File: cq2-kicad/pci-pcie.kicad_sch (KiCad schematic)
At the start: 52 parts, among them U6 PI7C9X111, U7 24LC02B

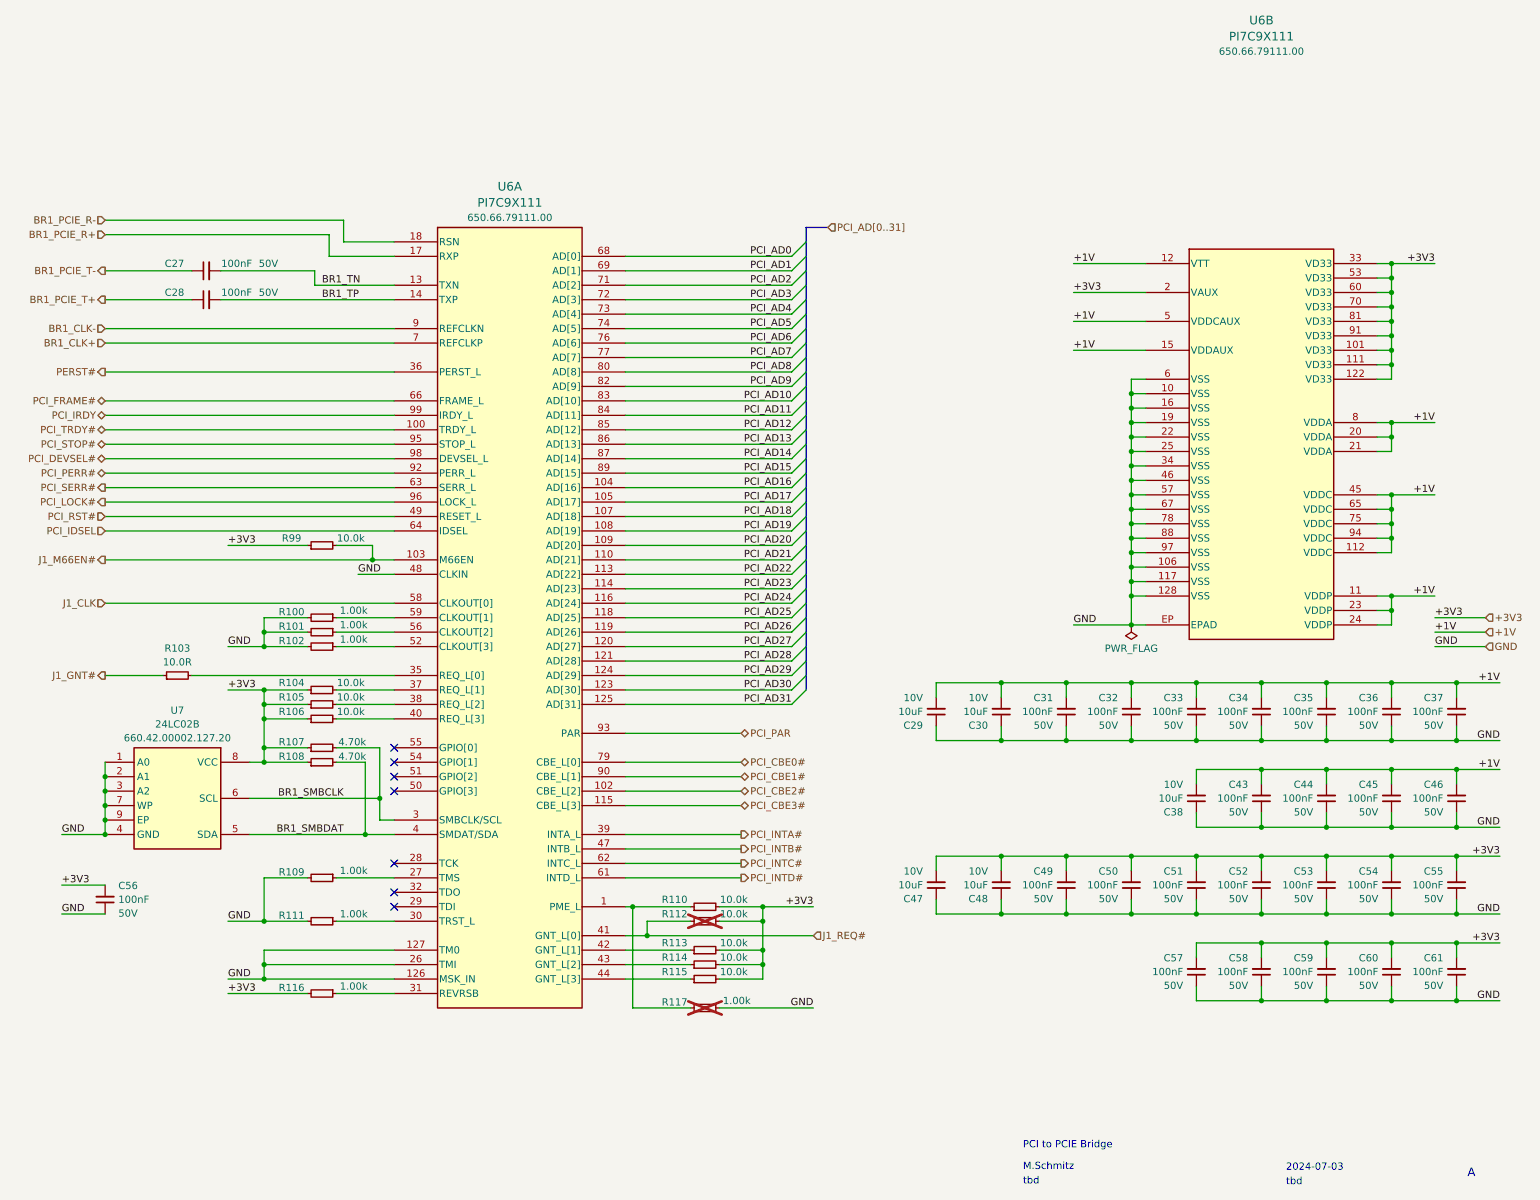
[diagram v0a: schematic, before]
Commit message: drc checked before panalization
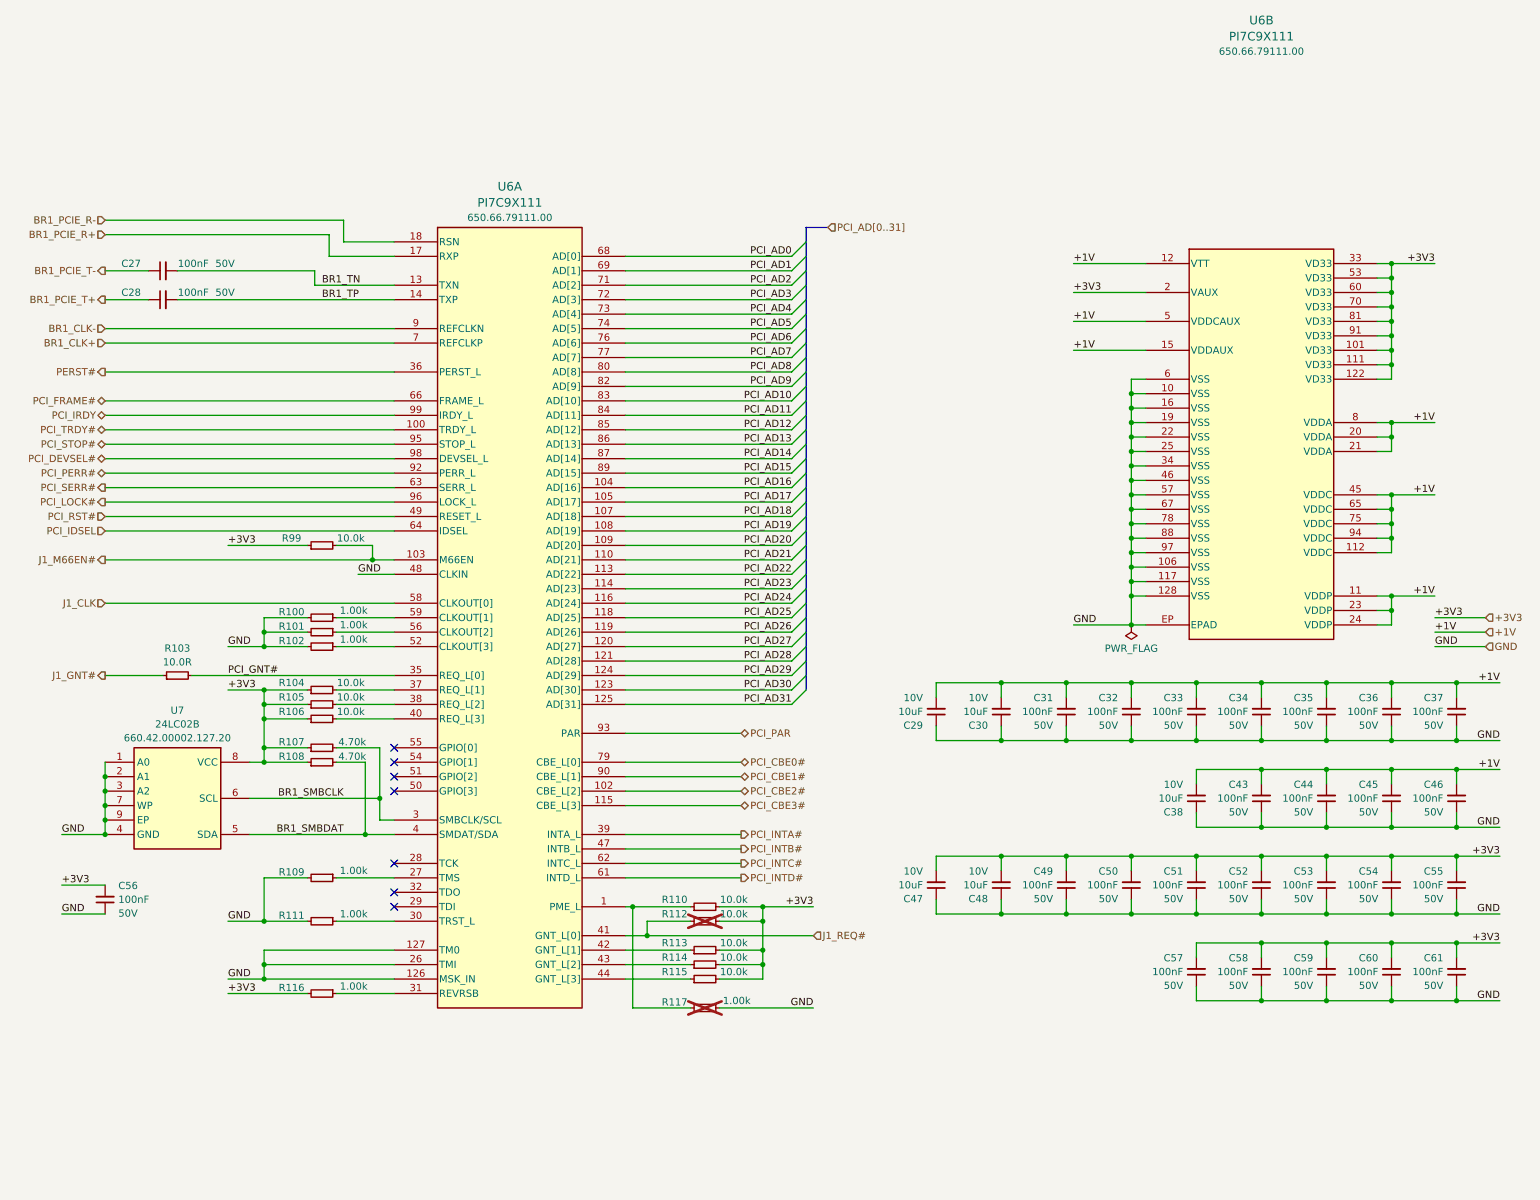
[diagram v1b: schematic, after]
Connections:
- net PCI_GNT#: now reaches R103.2, U6.35 (REQ_L[0])
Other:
- note removed: "2024-07-03"
- note removed: "A"
- note removed: "M.Schmitz"
- note removed: "PCI to PCIE Bridge"
- note removed: "tbd"
- title: (none) -> CQ2
- moved on the sheet: C27, C28
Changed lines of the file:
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@@
 	(paper "A4")
 	(title_block
-		(date "2024-07-17")
+		(title "CQ2")
+		(date "2024-07-31")
 		(rev "0")
+		(comment 1 "PCI to PCIE Bridge")
+		(comment 2 "Manfred Schmitz")
+		(comment 3 "tbd")
+		(comment 4 "202-07-03")
+		(comment 5 "tbd")
+		(comment 6 "A")
 	)
 	(junction
@@
 	(wire
 		(pts
-			(xy 49.53 38.1) (xy 80.01 38.1)
+			(xy 41.91 38.1) (xy 80.01 38.1)
 		)
 		(stroke
@@
 	(wire
 		(pts
-			(xy 29.21 33.02) (xy 44.45 33.02)
+			(xy 29.21 33.02) (xy 36.83 33.02)
 		)
 		(stroke
@@
 	(wire
 		(pts
-			(xy 29.21 38.1) (xy 44.45 38.1)
+			(xy 29.21 38.1) (xy 36.83 38.1)
 		)
 		(stroke
@@
 	(wire
 		(pts
-			(xy 66.04 33.02) (xy 49.53 33.02)
+			(xy 66.04 33.02) (xy 41.91 33.02)
 		)
 		(stroke
@@
 		)
 	)
-	(text "M.Schmitz"
-		(exclude_from_sim no)
-		(at 190.5 191.262 0)
-		(effects
-			(font
-				(size 1.27 1.27)
-			)
-			(justify left bottom)
-		)
-	)
-	(text "A"
-		(exclude_from_sim no)
-		(at 268.605 192.532 0)
-		(effects
-			(font
-				(size 1.4986 1.4986)
-			)
-			(justify left bottom)
-		)
-	)
-	(text "tbd"
-		(exclude_from_sim no)
-		(at 190.5 193.802 0)
-		(effects
-			(font
-				(size 1.27 1.27)
-			)
-			(justify left bottom)
-		)
-	)
-	(text "PCI to PCIE Bridge"
-		(exclude_from_sim no)
-		(at 190.5 187.452 0)
-		(effects
-			(font
-				(size 1.27 1.27)
-			)
-			(justify left bottom)
-		)
-	)
-	(text "tbd"
-		(exclude_from_sim no)
-		(at 236.728 193.929 0)
-		(effects
-			(font
-				(size 1.27 1.27)
-			)
-			(justify left bottom)
-		)
-	)
-	(text "2024-07-03"
-		(exclude_from_sim no)
-		(at 236.728 191.389 0)
-		(effects
-			(font
-				(size 1.27 1.27)
-			)
-			(justify left bottom)
-		)
-	)
 	(label "PCI_AD3"
 		(at 149.86 38.1 180)
@@
 		)
 	)
+	(label "PCI_GNT#"
+		(at 50.8 104.14 0)
+		(fields_autoplaced yes)
+		(effects
+			(font
+				(size 1.27 1.27)
+			)
+			(justify left bottom)
+		)
+	)
 	(label "PCI_AD30"
 		(at 149.86 106.68 180)
@@
 		)
 	)
+	(netclass_flag ""
+		(length 1.28)
+		(shape round)
+		(at 57.15 38.1 0)
+		(effects
+			(font
+				(size 1.27 1.27)
+			)
+			(justify left bottom)
+		)
+		(property "Netclass" "PCIE"
+			(at 57.658 36.83 0)
+			(effects
+				(font
+					(size 1.27 1.27)
+					(italic yes)
+				)
+				(justify left)
+			)
+		)
+	)
+	(netclass_flag ""
+		(length 1.28)
+		(shape round)
+		(at 57.15 33.02 0)
+		(effects
+			(font
+				(size 1.27 1.27)
+			)
+			(justify left bottom)
+		)
+		(property "Netclass" "PCIE"
+			(at 57.658 31.75 0)
+			(effects
+				(font
+					(size 1.27 1.27)
+					(italic yes)
+				)
+				(justify left)
+			)
+		)
+	)
 	(symbol
 		(lib_id "ci4rail-database:capacitors/86")
@@
 	(symbol
 		(lib_id "ci4rail-database:capacitors/86")
-		(at 46.99 33.02 90)
+		(at 39.37 33.02 90)
 		(unit 1)
 		(exclude_from_sim no)
@@
 		(dnp no)
 		(property "Reference" "C27"
-			(at 41.402 31.75 90)
+			(at 33.782 31.75 90)
 			(effects
 				(font
@@
 		)
 		(property "Value" "100nF"
-			(at 52.324 31.75 90)
+			(at 44.704 31.75 90)
 			(effects
 				(font
@@
 		)
 		(property "Footprint" "0-standard:0402-capacitor"
-			(at 46.99 33.02 0)
+			(at 39.37 33.02 0)
 			(effects
 				(font
@@
 		)
 		(property "Datasheet" ""
-			(at 46.99 33.02 0)
+			(at 39.37 33.02 0)
 			(effects
 				(font
@@
 		)
 		(property "Description" "Multilayer Ceramic Capacitors"
-			(at 46.99 33.02 0)
+			(at 39.37 33.02 0)
 			(effects
 				(font
@@
 		)
 		(property "Value1" "+/-10 %"
-			(at 46.99 33.02 0)
+			(at 39.37 33.02 0)
 			(effects
 				(font
@@
 		)
 		(property "Value2" "50V"
-			(at 57.912 31.75 90)
+			(at 50.292 31.75 90)
 			(effects
 				(font
@@
 		)
 		(property "Value3" "X5R/X7R"
-			(at 46.99 33.02 0)
+			(at 39.37 33.02 0)
 			(effects
 				(font
@@
 		)
 		(property "Value4" ""
-			(at 46.99 33.02 0)
+			(at 39.37 33.02 0)
 			(effects
 				(font
@@
 		)
 		(property "MPN" "n/a"
-			(at 46.99 33.02 0)
+			(at 39.37 33.02 0)
 			(effects
 				(font
@@
 		)
 		(property "MPN1" ""
-			(at 46.99 33.02 0)
+			(at 39.37 33.02 0)
 			(effects
 				(font
@@
 		)
 		(property "MPN2" ""
-			(at 46.99 33.02 0)
+			(at 39.37 33.02 0)
 			(effects
 				(font
@@
 		)
 		(property "LTB" "9999"
-			(at 46.99 33.02 0)
+			(at 39.37 33.02 0)
 			(effects
 				(font
@@
 		)
 		(property "ERP1" "M120-00060-00"
-			(at 46.99 33.02 0)
+			(at 39.37 33.02 0)
 			(effects
 				(font
@@
 		)
 		(property "ERP2" "110.42.410.050.0"
-			(at 46.99 33.02 0)
+			(at 39.37 33.02 0)
 			(effects
 				(font
@@
 		)
 		(property "Cost" "0.02"
-			(at 46.99 33.02 0)
+			(at 39.37 33.02 0)
 			(effects
 				(font
@@
 		)
 		(property "Lifecycle" "released"
-			(at 46.99 33.02 0)
+			(at 39.37 33.02 0)
 			(effects
 				(font
@@
 		)
 		(property "Outline" "SMT 0402"
-			(at 46.99 33.02 0)
+			(at 39.37 33.02 0)
 			(effects
 				(font
@@
 	(symbol
 		(lib_id "ci4rail-database:capacitors/86")
-		(at 46.99 38.1 90)
+		(at 39.37 38.1 90)
 		(unit 1)
 		(exclude_from_sim no)
@@
 		(dnp no)
 		(property "Reference" "C28"
-			(at 41.402 36.83 90)
+			(at 33.782 36.83 90)
 			(effects
 				(font
@@
 		)
 		(property "Value" "100nF"
-			(at 52.324 36.83 90)
+			(at 44.704 36.83 90)
 			(effects
 				(font
@@
 		)
 		(property "Footprint" "0-standard:0402-capacitor"
-			(at 46.99 38.1 0)
+			(at 39.37 38.1 0)
 			(effects
 				(font
@@
 		)
 		(property "Datasheet" ""
-			(at 46.99 38.1 0)
+			(at 39.37 38.1 0)
 			(effects
 				(font
@@
 		)
 		(property "Description" "Multilayer Ceramic Capacitors"
-			(at 46.99 38.1 0)
+			(at 39.37 38.1 0)
 			(effects
 				(font
@@
 		)
 		(property "Value1" "+/-10 %"
-			(at 46.99 38.1 0)
+			(at 39.37 38.1 0)
 			(effects
 				(font
@@
 		)
 		(property "Value2" "50V"
-			(at 57.912 36.83 90)
+			(at 50.292 36.83 90)
 			(effects
 				(font
@@
 		)
 		(property "Value3" "X5R/X7R"
-			(at 46.99 38.1 0)
+			(at 39.37 38.1 0)
 			(effects
 				(font
@@
 		)
 		(property "Value4" ""
-			(at 46.99 38.1 0)
+			(at 39.37 38.1 0)
 			(effects
 				(font
@@
 		)
 		(property "MPN" "n/a"
-			(at 46.99 38.1 0)
+			(at 39.37 38.1 0)
 			(effects
 				(font
@@
 		)
 		(property "MPN1" ""
-			(at 46.99 38.1 0)
+			(at 39.37 38.1 0)
 			(effects
 				(font
@@
 		)
 		(property "MPN2" ""
-			(at 46.99 38.1 0)
+			(at 39.37 38.1 0)
 			(effects
 				(font
@@
 		)
 		(property "LTB" "9999"
-			(at 46.99 38.1 0)
+			(at 39.37 38.1 0)
 			(effects
 				(font
@@
 		)
 		(property "ERP1" "M120-00060-00"
-			(at 46.99 38.1 0)
+			(at 39.37 38.1 0)
 			(effects
 				(font
@@
 		)
 		(property "ERP2" "110.42.410.050.0"
-			(at 46.99 38.1 0)
+			(at 39.37 38.1 0)
 			(effects
 				(font
@@
 		)
 		(property "Cost" "0.02"
-			(at 46.99 38.1 0)
+			(at 39.37 38.1 0)
 			(effects
 				(font
@@
 		)
 		(property "Lifecycle" "released"
-			(at 46.99 38.1 0)
+			(at 39.37 38.1 0)
 			(effects
 				(font
@@
 		)
 		(property "Outline" "SMT 0402"
-			(at 46.99 38.1 0)
+			(at 39.37 38.1 0)
 			(effects
 				(font

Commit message: Production documents created
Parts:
- U6: Lifecycle review pending CQ2 -> ERP1 pending CQ2
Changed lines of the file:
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@@
 	(title_block
 		(title "CQ2")
-		(date "2024-07-31")
+		(date "2024-08-03")
 		(rev "0")
 		(comment 1 "PCI to PCIE Bridge")
@@
 	)
 	(symbol
-		(lib_name "integrated/145_1")
 		(lib_id "ci4rail-database:integrated/145")
 		(at 100.33 93.98 0)
@@
 			)
 		)
-		(property "Lifecycle" "review pending CQ2"
+		(property "Lifecycle" "ERP1 pending CQ2"
 			(at 100.33 93.98 0)
 			(effects

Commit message: Production documents new
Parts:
- U6: Lifecycle review pending CQ2 -> ERP1 pending CQ2; Outline (none) -> SMT LQFP128 14x14x1.45mm
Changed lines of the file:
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@@
 		(fields_autoplaced yes)
 		(property "Reference" "U6"
-			(at 232.41 -10.9916 0)
+			(at 232.41 22.0284 0)
 			(effects
 				(font
@@
 		)
 		(property "Value" "PI7C9X111"
-			(at 232.41 -8.1587 0)
+			(at 232.41 24.8613 0)
 			(effects
 				(font
@@
 		)
 		(property "ERP2" "650.66.79111.00"
-			(at 232.41 -5.5301 0)
+			(at 232.41 27.4899 0)
 			(effects
 				(font
@@
 			)
 		)
-		(property "Lifecycle" "review pending CQ2"
+		(property "Lifecycle" "ERP1 pending CQ2"
 			(at 232.41 64.77 0)
 			(effects
@@
 			)
 		)
-		(property "Outline" ""
+		(property "Outline" "SMT LQFP128 14x14x1.45mm"
 			(at 232.41 64.77 0)
 			(effects
